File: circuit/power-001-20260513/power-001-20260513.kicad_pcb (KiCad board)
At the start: 2 copper layers, 68.4 x 46.4 mm, 50 parts, among them J1 VIN, J2 +5V_{Line}, J3 Power, J4 Logic, J5 Sub_{Power}, J6 Sub_{Signal}, J7 ICSP_{PIC12F683}, Q1 BSS138, Q2 PMOS, SW1 SW_SPDT, SW2 SW_SPDT, SW3 SW_SPDT, SW4 Locker_SW, U1 OKL-T/6-W12N-C, U2 OKL-T/6-W12N-C, U3 AZ1084-3.3, U5 PIC12F683-xSN, U6 LM1117MP-3.3

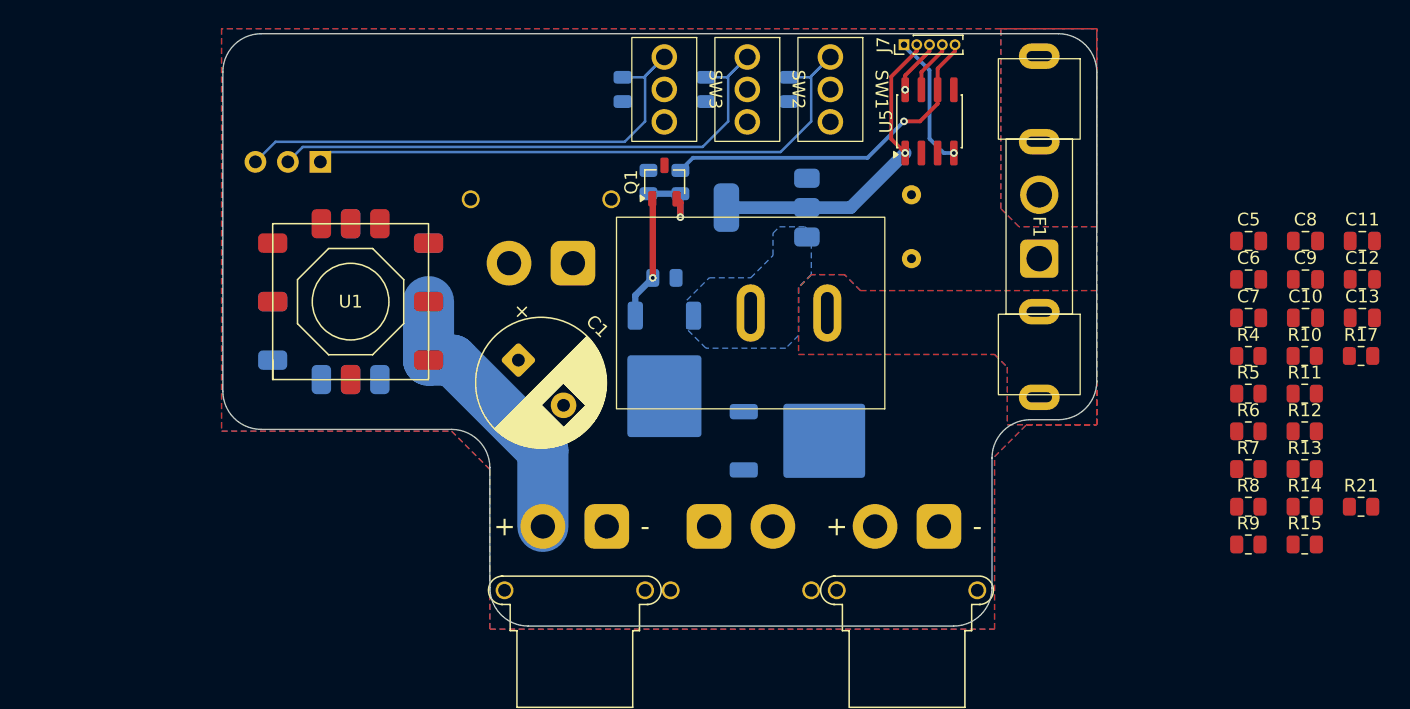
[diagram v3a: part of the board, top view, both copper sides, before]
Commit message: Update 電源基板のPCBを進めた
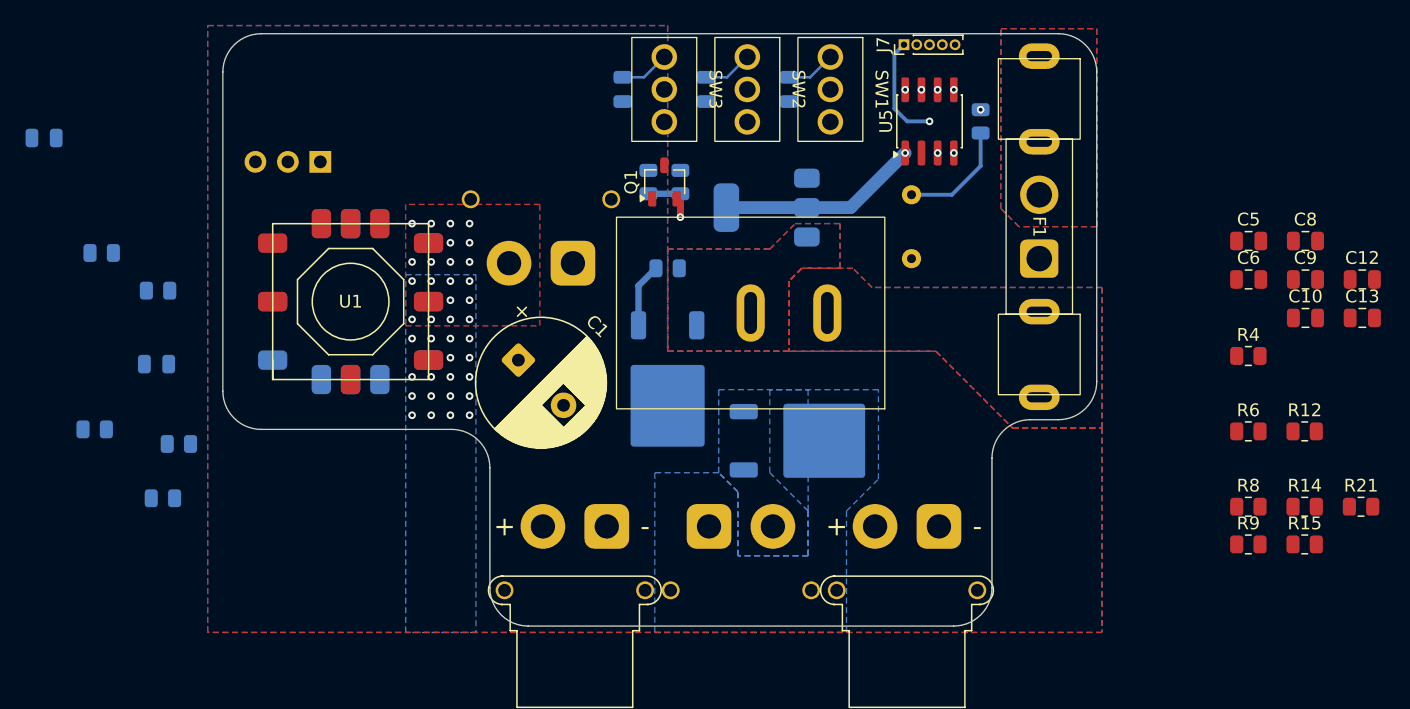
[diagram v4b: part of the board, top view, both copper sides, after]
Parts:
- C11, C7, R10, R11, R13, R17, R5, R7: moved to B.Cu
- moved C11 103.5 mm to (-55.3, -13.7), turned to 180 degrees
- moved R10 94.5 mm to (-50.8, -4.70), turned to 180 degrees
- moved R7 90.3 mm to (-51.3, 9.11), turned to 180 degrees
- moved R13 89.4 mm to (-46.0, 14.5), turned to 180 degrees
- moved R11 88.2 mm to (-44.8, 10.2), turned to 180 degrees
- moved R5 85.7 mm to (-46.4, -1.75), turned to 180 degrees
- moved C7 85.6 mm to (-46.5, 4.00), turned to 180 degrees
- moved R17 35.0 mm to (18.0, -15.0), turned to 90 degrees
- moved Q2 0.79 mm to (-6.50, 6.00)
- moved R20 0.79 mm to (-6.50, -3.50)
- turned BZ1 to -90 degrees
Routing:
- net SW_TGL_1: track 49.3 -> 3.91 mm
- net SW_TGL_2: track 45.3 -> 3.91 mm
- net SW_TGL_3: track 41.4 -> 3.91 mm
- net ICSPCLK: track 27.5 -> 4.09 mm
- net +5V_{Line}: track 22.4 -> 0.00 mm, vias 0 -> 22
- net Net-(BZ1-+): track 0.00 -> 8.93 mm
- net Net-(Q1-D): track 9.73 -> 5.03 mm, vias 1 -> 0
- net GND: track 4.31 -> 0.00 mm
- net Prot-Buzzer: track 0.00 -> 2.74 mm, vias 0 -> 2
- net MCLR: track 10.6 -> 11.7 mm, vias 1 -> 2
- net ICSPDAT: vias 0 -> 1
- net Prot-LED: vias 0 -> 1
- net +5V: vias 0 -> 16
- added copper zone on B.Cu, net +3.3V
- added copper zone on B.Cu, net +5V
- added copper zone on F.Cu, net +5V
- added copper zone on In1.Cu, net +5V
- added copper zone on In2.Cu, net +5V
- added copper zone on B.Cu, net +5V_{Line}
- added copper zone on In1.Cu, net +5V_{Line}
- added copper zone on In2.Cu, net +5V_{Line}
- added copper zone on In1.Cu, net GND
- added copper zone on In2.Cu, net GND
- added copper zone on F.Cu, net VCC
- added copper zone on B.Cu, net VIN
- added copper zone on F.Cu, net VIN
- removed copper zone on B.Cu, net GND
- removed copper zone on F.Cu, net GND
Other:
- copper layers 2 -> 4

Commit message: Update 電源基板のボード図作成終わり！！！！
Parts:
- added J8: ESC, @Thrive_footprint_power:Conn_01x02_Wire_Only_SMD, B.Cu at (16.0, 8.50)
- C10, C12, C13, C5, C6, C8, C9, R12, R14, R15, R21, R4, R6, R8, R9: moved to B.Cu
- moved R12 77.8 mm to (-29.5, -18.0), turned to 180 degrees
- moved R4 75.6 mm to (-36.5, 7.50), turned to 180 degrees
- moved C10 74.7 mm to (-29.5, -16.0), turned to 180 degrees
- moved R9 72.6 mm to (-23.5, -19.0), turned to 180 degrees
- moved R6 70.9 mm to (-26.5, -18.0), turned to -90 degrees
- moved R8 70.2 mm to (-23.5, -17.0)
- moved C6 68.9 mm to (-29.5, -10.0)
- moved R21 51.3 mm to (9.50, -19.0), turned to -90 degrees
- moved C8 46.6 mm to (-0.50, 10.1), turned to 180 degrees
- moved R14 46.3 mm to (1.00, -3.50)
- moved R15 44.5 mm to (4.50, -3.50)
- moved C5 43.5 mm to (-4.50, -5.00), turned to 90 degrees
- moved C13 41.3 mm to (9.50, -15.0), turned to 90 degrees
- moved R13 38.2 mm to (-29.5, -20.0)
- moved C9 35.3 mm to (10.5, 10.0), turned to 90 degrees
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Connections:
- U5 pad 3: Prot-LED -> unconnected-(U5-GP4-Pad3)
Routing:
- net SW_TGL_1: track 3.91 -> 49.2 mm
- net SW_TGL_2: track 3.91 -> 45.2 mm
- net SW_TGL_3: track 3.91 -> 39.3 mm
- net ICSPDAT: track 4.20 -> 33.7 mm, vias 1 -> 2
- net Net-(U1-Trim): track 0.00 -> 23.3 mm, vias 0 -> 2
- net ICSPCLK: track 4.09 -> 26.6 mm, vias 1 -> 2
- net +5V_{Line}: track 0.00 -> 21.9 mm, vias 22 -> 21
- net +5V: track 0.00 -> 14.6 mm, vias 16 -> 18
- net GND: track 0.00 -> 11.2 mm, vias 1 -> 56
- net +3.3VA: track 25.3 -> 33.8 mm, vias 1 -> 2
- net Net-(Q1-D): track 5.03 -> 10.8 mm, vias 0 -> 1
- net Net-(U2-Trim): track 0.00 -> 5.23 mm
- net +3.3V: track 0.00 -> 5.13 mm
- net Net-(R11-Pad2): track 0.00 -> 2.76 mm
- net MCLR: track 11.7 -> 14.0 mm
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- added copper zone on B.Cu, net GND
- added copper zone on F.Cu, net GND

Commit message: Update 電源基板の寸法変更を確認
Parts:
- moved C2 0.26 mm to (3.25, -17.5)
- moved C3 0.26 mm to (-3.25, -17.5)
- moved SW2 0.26 mm to (0.00, -17.5)
- moved C4 0.26 mm to (-9.75, -17.5)
- moved SW1 0.26 mm to (6.50, -17.5)
- moved SW3 0.26 mm to (-6.50, -17.5)
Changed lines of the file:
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@@
 	(footprint "@Thrive_footprint_power:2MS1-T1-B4-M2-Q-E"
 		(layer "F.Cu")
-		(at 6.239696 -17.499998 -90)
+		(at 6.5 -17.5 -90)
 		(property "Reference" "SW1"
 			(at 0 -4 270)
@@
 	(footprint "@Thrive_footprint_power:2MS1-T1-B4-M2-Q-E"
 		(layer "F.Cu")
-		(at -6.760304 -17.499998 -90)
+		(at -6.5 -17.5 -90)
 		(property "Reference" "SW3"
 			(at 0 -4 270)
@@
 	(footprint "@Thrive_footprint_power:2MS1-T1-B4-M2-Q-E"
 		(layer "F.Cu")
-		(at -0.260304 -17.499998 -90)
+		(at 0 -17.5 -90)
 		(property "Reference" "SW2"
 			(at 0 -4 270)
@@
 	(footprint "Capacitor_SMD:C_0805_2012Metric"
 		(layer "B.Cu")
-		(at -10.010304 -17.499998 -90)
+		(at -9.75 -17.5 -90)
 		(descr "Capacitor SMD 0805 (2012 Metric), square (rectangular) end terminal, IPC-7351 nominal, (Body size source: IPC-SM-782 page 76, https://www.pcb-3d.com/wordpress/wp-content/uploads/ipc-sm-782a_amendment_1_and_2.pdf, https://docs.google.com/spreadsheets/d/1BsfQQcO9C6DZCsRaXUlFlo91Tg2WpOkGARC1WS5S8t0/edit?usp=sharing)")
 		(tags "capacitor")
@@
 	(footprint "Capacitor_SMD:C_0805_2012Metric"
 		(layer "B.Cu")
-		(at -3.510304 -17.499998 -90)
+		(at -3.25 -17.5 -90)
 		(descr "Capacitor SMD 0805 (2012 Metric), square (rectangular) end terminal, IPC-7351 nominal, (Body size source: IPC-SM-782 page 76, https://www.pcb-3d.com/wordpress/wp-content/uploads/ipc-sm-782a_amendment_1_and_2.pdf, https://docs.google.com/spreadsheets/d/1BsfQQcO9C6DZCsRaXUlFlo91Tg2WpOkGARC1WS5S8t0/edit?usp=sharing)")
 		(tags "capacitor")
@@
 	(footprint "Capacitor_SMD:C_0805_2012Metric"
 		(layer "B.Cu")
-		(at 2.989696 -17.499998 -90)
+		(at 3.25 -17.5 -90)
 		(descr "Capacitor SMD 0805 (2012 Metric), square (rectangular) end terminal, IPC-7351 nominal, (Body size source: IPC-SM-782 page 76, https://www.pcb-3d.com/wordpress/wp-content/uploads/ipc-sm-782a_amendment_1_and_2.pdf, https://docs.google.com/spreadsheets/d/1BsfQQcO9C6DZCsRaXUlFlo91Tg2WpOkGARC1WS5S8t0/edit?usp=sharing)")
 		(tags "capacitor")
@@
 	)
 	(segment
-		(start 4.649695 -18.449997)
-		(end 2.989696 -18.449997)
+		(start 6.5 -20.04)
+		(end 4.909997 -18.449997)
 		(width 0.3)
 		(layer "B.Cu")
@@
 	)
 	(segment
-		(start 6.239696 -20.039998)
-		(end 4.649695 -18.449997)
+		(start 3.250002 -18.449997)
+		(end 3.25 -18.449999)
 		(width 0.3)
 		(layer "B.Cu")
@@
 	)
 	(segment
-		(start -32.400772 -13.109998)
-		(end 2.609998 -13.109998)
+		(start 4.909997 -18.449997)
+		(end 3.250002 -18.449997)
 		(width 0.3)
-		(layer "In2.Cu")
+		(layer "B.Cu")
 		(net "SW_TGL_1")
 	)
 	(segment
-		(start 2.609998 -13.109998)
-		(end 4.5 -15)
+		(start 4.75 -18.29)
+		(end 6.5 -20.04)
 		(width 0.3)
 		(layer "In2.Cu")
@@
 	)
 	(segment
-		(start 4.5 -15)
-		(end 4.5 -18.300302)
+		(start 4.75 -15.25)
+		(end 4.75 -18.29)
 		(width 0.3)
 		(layer "In2.Cu")
@@
 	)
 	(segment
-		(start 4.5 -18.300302)
-		(end 6.239696 -20.039998)
+		(start -32.400772 -13.109998)
+		(end 2.609998 -13.109998)
+		(width 0.3)
+		(layer "In2.Cu")
+		(net "SW_TGL_1")
+	)
+	(segment
+		(start 2.609998 -13.109998)
+		(end 4.75 -15.25)
 		(width 0.3)
 		(layer "In2.Cu")
@@
 	)
 	(segment
-		(start 11.025001 -12.525)
-		(end 12.095 -12.525)
-		(width 1)
+		(start 9.5 -18.0875)
+		(end 8 -16.5875)
+		(width 0.5)
 		(layer "B.Cu")
 		(net "+3.3VA")
 	)
 	(segment
-		(start 4.399999 -8.25)
-		(end -1.899999 -8.25)
+		(start 11.025001 -12.525)
+		(end 12.095 -12.525)
 		(width 1)
 		(layer "B.Cu")
@@
 	)
 	(segment
-		(start 9.5 -18.0875)
-		(end 8 -16.5875)
-		(width 0.5)
-		(layer "B.Cu")
-		(net "+3.3VA")
-	)
-	(segment
-		(start 9.5 -14.050001)
-		(end 11.025001 -12.525)
+		(start 4.399999 -8.25)
+		(end -1.899999 -8.25)
 		(width 1)
 		(layer "B.Cu")
@@
 	)
 	(segment
+		(start 9.5 -14.050001)
+		(end 11.025001 -12.525)
+		(width 1)
+		(layer "B.Cu")
+		(net "+3.3VA")
+	)
+	(segment
 		(start 11.25 -13.37)
 		(end 12.095 -12.525)
@@
 	)
 	(segment
-		(start -8.350305 -18.449997)
-		(end -10.010304 -18.449997)
+		(start -6.5 -20.04)
+		(end -8.090003 -18.449997)
+		(width 0.3)
+		(layer "B.Cu")
+		(net "SW_TGL_3")
+	)
+	(segment
+		(start -9.749998 -18.449997)
+		(end -9.75 -18.449999)
 		(width 0.3)
 		(layer "B.Cu")
@@
 	)
 	(segment
-		(start -6.760304 -20.039998)
-		(end -8.350305 -18.449997)
+		(start -8.090003 -18.449997)
+		(end -9.749998 -18.449997)
 		(width 0.3)
 		(layer "B.Cu")
@@
 	)
 	(segment
-		(start -6.760304 -20.039998)
-		(end -12.690304 -14.109998)
+		(start -6.5 -20.04)
+		(end -12.430002 -14.109998)
 		(width 0.3)
 		(layer "In2.Cu")
@@
 	)
 	(segment
-		(start -12.690304 -14.109998)
+		(start -12.430002 -14.109998)
 		(end -36.480772 -14.109998)
 		(width 0.3)
@@
 	)
 	(segment
-		(start -0.260304 -20.039998)
-		(end -1.850305 -18.449997)
+		(start -3.25 -18.449999)
+		(end -3.250002 -18.449997)
 		(width 0.3)
 		(layer "B.Cu")
@@
 	)
 	(segment
-		(start -1.850305 -18.449997)
-		(end -3.510304 -18.449997)
+		(start 0 -20.04)
+		(end -1.590001 -18.449999)
 		(width 0.3)
 		(layer "B.Cu")
@@
 	)
 	(segment
-		(start -34.440772 -13.609998)
-		(end -3.390002 -13.609998)
+		(start -1.590001 -18.449999)
+		(end -3.25 -18.449999)
+		(width 0.3)
+		(layer "B.Cu")
+		(net "SW_TGL_2")
+	)
+	(segment
+		(start -1.75 -18.29)
+		(end 0 -20.04)
 		(width 0.3)
 		(layer "In2.Cu")
@@
 	)
 	(segment
-		(start -2 -15)
-		(end -2 -18.300302)
+		(start -34.440772 -13.609998)
+		(end -3.390002 -13.609998)
 		(width 0.3)
 		(layer "In2.Cu")
@@
 	)
 	(segment
-		(start -2 -18.300302)
-		(end -0.260304 -20.039998)
+		(start -3.390002 -13.609998)
+		(end -1.75 -15.25)
 		(width 0.3)
 		(layer "In2.Cu")
@@
 	)
 	(segment
-		(start -3.390002 -13.609998)
-		(end -2 -15)
+		(start -1.75 -15.25)
+		(end -1.75 -18.29)
 		(width 0.3)
 		(layer "In2.Cu")

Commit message: Update 電源基板いったん完成、シルクスクリーンだけきれいにしなきゃ
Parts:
- removed C4: 100n, Capacitor_SMD:C_0805_2012Metric
- removed SW3: SW_SPDT, @Thrive_footprint_power:2MS1-T1-B4-M2-Q-E
- J6: footprint Connector_PinHeader_2.54mm:PinHeader_1x03_P2.54mm_Horizontal -> Connector_PinHeader_2.54mm:PinHeader_1x02_P2.54mm_Horizontal
- moved C3 4.25 mm to (-7.50, -17.5)
- moved SW2 4.25 mm to (-4.25, -17.5)
- moved C2 2.25 mm to (1.00, -17.5)
- moved SW1 2.25 mm to (4.25, -17.5)
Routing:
- net SW_TGL_3: track 39.6 -> 0.00 mm
- net SW_TGL_2: track 45.3 -> 39.3 mm
- net SW_TGL_1: track 49.3 -> 45.2 mm

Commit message: Update 電源基板のシルクを整えた
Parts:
- Q2: value PMOS -> TJ60S04M3L
- R10: value 1.5k -> 1k
- U5: value PIC12F683-xSN -> PIC12F683
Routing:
- net GND: vias 56 -> 171
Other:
- board text added: "Power-001"
